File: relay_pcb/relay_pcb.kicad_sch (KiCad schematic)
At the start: 4 parts, among them J1 703W-00_52, J2 1984963, J3 1984963, K1 EE2-5TNUH-L

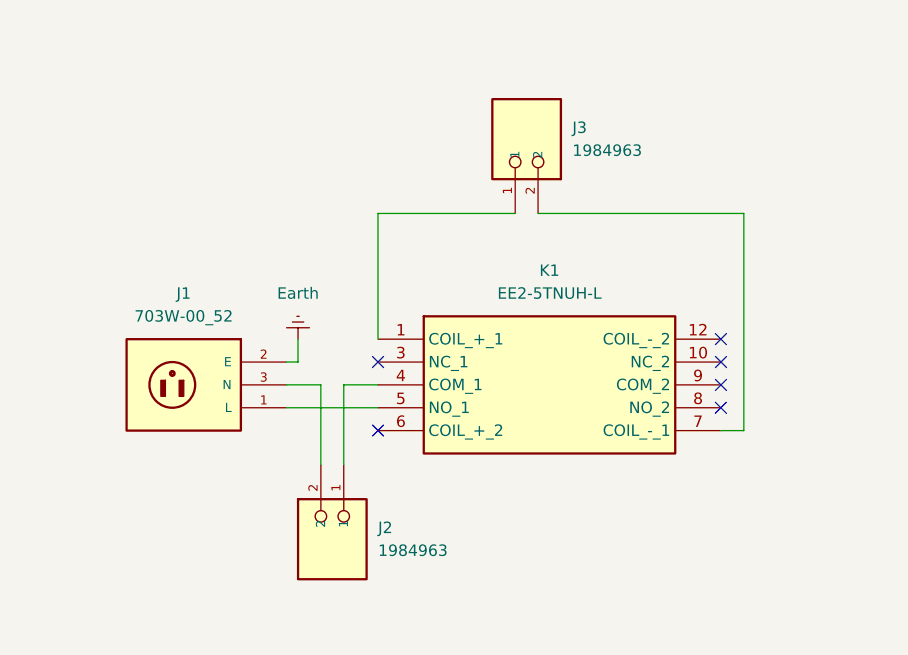
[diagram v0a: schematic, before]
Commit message: kicad: relay pcb board for turning on lighbulb 120VAC with +5V
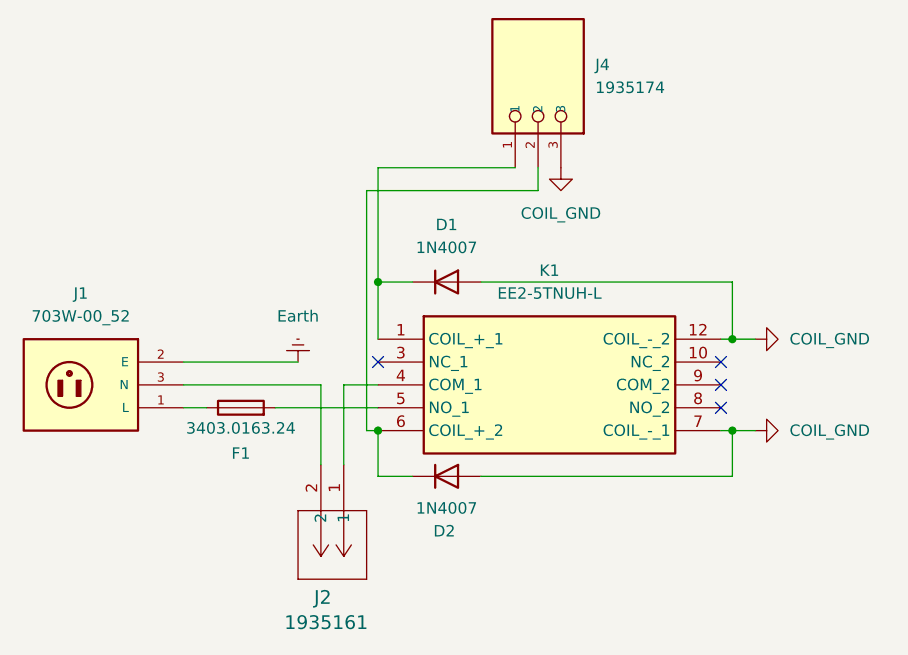
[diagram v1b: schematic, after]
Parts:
- removed J2, J3: 1984963, 1984963:PHOENIX_1984963, symbol CONN_1984963:1984963
- added D1, D2: 1N4007, Diode_THT:D_DO-41_SOD81_P7.62mm_Horizontal, symbol Device:D
- added F1: 3403.0163.24, Fuse:Fuse_2010_5025Metric, symbol Device:Fuse
- added J2: 1935161, vendor_eda:CONN_1935161_PXC, symbol CONN_1935161:1935161
- added J4: 1935174, vendor_eda:CONN_1935174_PXC, symbol CONN_1935174:1935174
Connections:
- net at J1.1 (L): now also F1.1; no longer K1.5 (NO_1)
- net at J1.3 (N): now also J2.2
- net at K1.1 (COIL_+_1): now also D1.1 (K), J4.1
- net COIL_GND: now reaches K1.12 (COIL_-_2)
- net COIL_GND: now also K1.7 (COIL_-_1), D1.2 (A), D2.2 (A), J4.3
- net at K1.4 (COM_1): now also J2.1
- net at K1.6 (COIL_+_2): now also D2.1 (K), J4.2
- new net: F1.2, K1.5 (NO_1)
- no-connect marks 6 -> 4
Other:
- moved on the sheet: J1
